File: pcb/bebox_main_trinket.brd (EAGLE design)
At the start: 92.8 x 35.2 mm, 25 parts, among them J1 SJ-435107RS, J2 SJ-435107RS, J4 SJ-435107RS, J6 PJ-102AH, P2 OSTTE020104, P3 OSTTE020104, P4 OSTTE020104, P5 OSTTE020104, T2 2SC2098V, T3 2SC2098V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

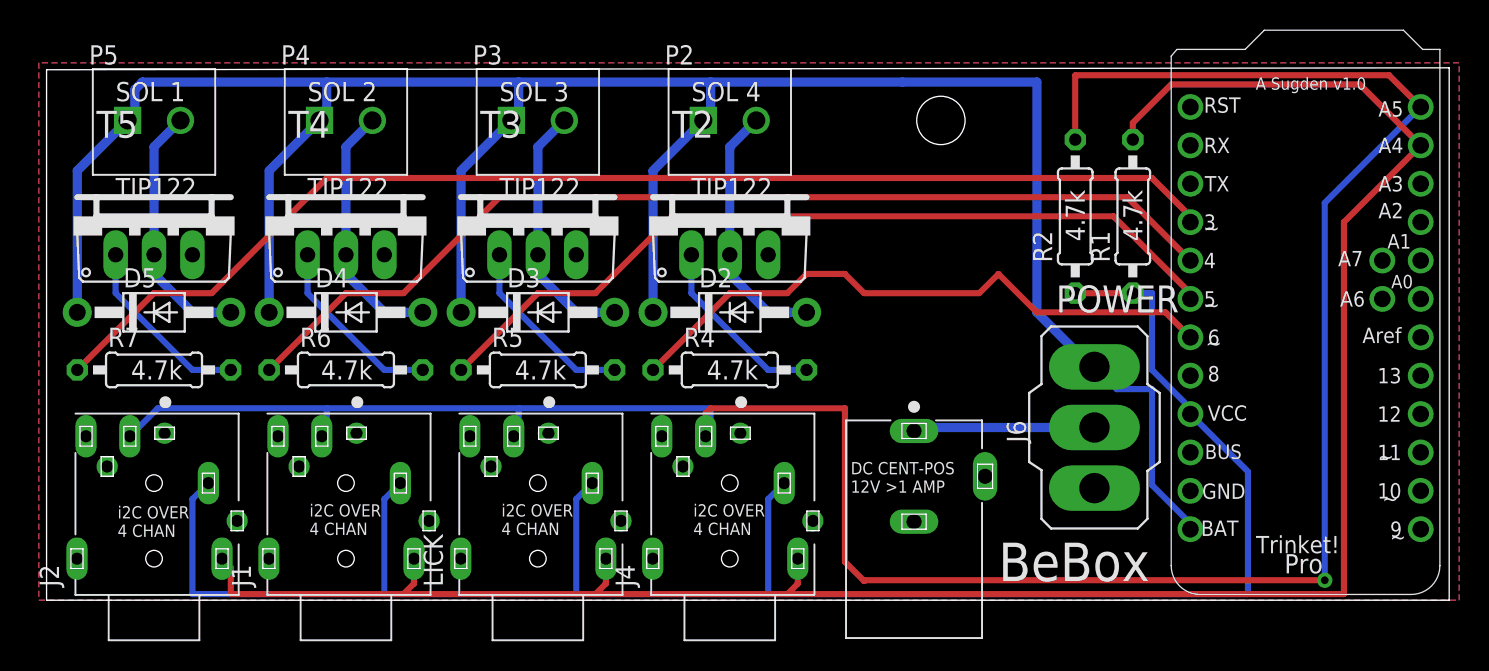
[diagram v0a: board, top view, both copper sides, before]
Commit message: Renamed original bebox main and udpated the  footprint of the switch.
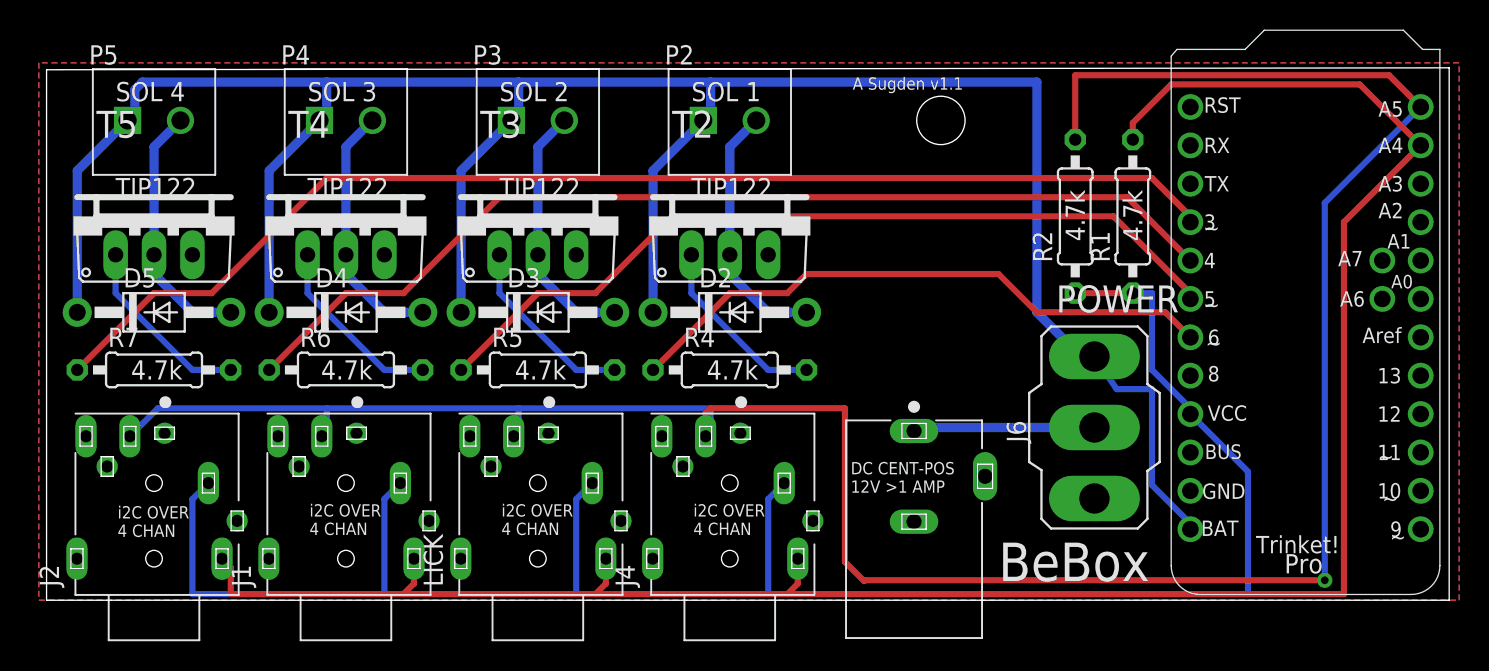
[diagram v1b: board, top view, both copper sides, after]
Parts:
- POWER: device switch:320-916 -> arthur:320-916
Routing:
- net N$15: track 41.0 -> 39.9 mm
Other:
- board text added: "A Sugden v1.1"
- board text removed: "A Sugden v1.0"
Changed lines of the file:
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@@
 <?xml version="1.0" encoding="utf-8"?>
 <!DOCTYPE eagle SYSTEM "eagle.dtd">
-<eagle version="9.3.0">
+<eagle version="9.3.2">
 <drawing>
 <settings>
@@
 <text x="13.97" y="36.83" size="1.27" layer="21">TIP122</text>
 <text x="72.39" y="11.43" size="2.54" layer="21">BeBox</text>
-<text x="89.408" y="43.942" size="0.8128" layer="21">A Sugden v1.0</text>
+<text x="62.738" y="43.942" size="0.8128" layer="21">A Sugden v1.1</text>
 <hole x="68.58" y="41.91" drill="3.199890625"/>
 <text x="14.097" y="14.351" size="0.8128" layer="21">i2C OVER
@@
 <text x="62.611" y="17.272" size="0.8128" layer="21">DC CENT-POS
 12V &gt;1 AMP</text>
-<text x="13.97" y="43.18" size="1.27" layer="21">SOL 1</text>
-<text x="26.67" y="43.18" size="1.27" layer="21">SOL 2</text>
-<text x="39.37" y="43.18" size="1.27" layer="21">SOL 3</text>
-<text x="52.07" y="43.18" size="1.27" layer="21">SOL 4</text>
+<text x="13.97" y="43.18" size="1.27" layer="21">SOL 4</text>
+<text x="26.67" y="43.18" size="1.27" layer="21">SOL 3</text>
+<text x="39.37" y="43.18" size="1.27" layer="21">SOL 2</text>
+<text x="52.07" y="43.18" size="1.27" layer="21">SOL 1</text>
 </plain>
 <attributes>
@@
 <attribute name="VALUE" x="12.20673125" y="36.706040625" size="1.27096875" layer="27"/>
 </element>
-<element name="POWER" library="switch" library_urn="urn:adsk.eagle:library:380" package="320-916" package3d_urn="urn:adsk.eagle:package:27678/1" value="" x="78.74" y="21.59" smashed="yes">
+<element name="POWER" library="arthur" package="320-916" package3d_urn="urn:adsk.eagle:package:27678/1" value="" x="78.74" y="21.59" smashed="yes">
 <attribute name="NAME" x="76.2" y="29.21" size="1.778" layer="25" ratio="10"/>
 <attribute name="VALUE" x="76.2" y="12.065" size="1.778" layer="27" ratio="10"/>
@@
 <wire x1="14.76" y1="41.91" x2="15.24" y2="42.39" width="0.6096" layer="16"/>
 <wire x1="15.24" y1="42.39" x2="15.24" y2="43.949509375" width="0.6096" layer="16"/>
-<wire x1="74.93" y1="29.21" x2="74.93" y2="44.45" width="0.6096" layer="16"/>
-<wire x1="74.93" y1="29.21" x2="78.5368" y2="25.6032" width="0.6096" layer="16"/>
-<wire x1="78.5368" y1="25.6032" x2="78.74" y2="25.6032" width="0.6096" layer="16"/>
+<wire x1="74.93" y1="44.45" x2="74.93" y2="29.21" width="0.6096" layer="16"/>
 <wire x1="15.740490625" y1="44.45" x2="15.24" y2="43.949509375" width="0.6096" layer="16"/>
-<wire x1="78.74" y1="25.6032" x2="80.2132" y2="24.13" width="0.4064" layer="16"/>
+<wire x1="78.74" y1="26.289" x2="80.2132" y2="24.13" width="0.4064" layer="16"/>
 <wire x1="80.2132" y1="24.13" x2="82.55" y2="24.13" width="0.4064" layer="16"/>
 <wire x1="82.55" y1="24.13" x2="82.55" y2="17.78" width="0.4064" layer="16"/>
@@
 <wire x1="49.53" y1="29.21" x2="49.53" y2="38.58" width="0.6096" layer="16"/>
 <wire x1="49.53" y1="38.58" x2="52.86" y2="41.91" width="0.6096" layer="16"/>
-<wire x1="74.93" y1="44.45" x2="66.04" y2="44.45" width="0.6096" layer="16"/>
-<wire x1="66.04" y1="44.45" x2="53.34" y2="44.45" width="0.6096" layer="16"/>
+<wire x1="74.93" y1="44.45" x2="53.34" y2="44.45" width="0.6096" layer="16"/>
 <wire x1="53.34" y1="44.45" x2="40.64" y2="44.45" width="0.6096" layer="16"/>
 <wire x1="40.64" y1="44.45" x2="27.94" y2="44.45" width="0.6096" layer="16"/>
@@
 <wire x1="40.16" y1="41.91" x2="40.64" y2="42.39" width="0.6096" layer="16"/>
 <wire x1="40.64" y1="42.39" x2="40.64" y2="44.45" width="0.6096" layer="16"/>
+<wire x1="74.93" y1="29.21" x2="77.851" y2="26.289" width="0.6096" layer="16"/>
+<wire x1="77.851" y1="26.289" x2="78.74" y2="26.289" width="0.6096" layer="16"/>
 </signal>
 <signal name="SDA">
@@
 <contactref element="U$1" pad="6"/>
 <wire x1="74.93" y1="29.21" x2="83.439" y2="29.21" width="0.4064" layer="1"/>
-<wire x1="74.93" y1="29.21" x2="72.39" y2="31.75" width="0.4064" layer="1"/>
-<wire x1="72.39" y1="31.75" x2="71.12" y2="30.48" width="0.4064" layer="1"/>
-<wire x1="71.12" y1="30.48" x2="63.5" y2="30.48" width="0.4064" layer="1"/>
-<wire x1="63.5" y1="30.48" x2="62.23" y2="31.75" width="0.4064" layer="1"/>
-<wire x1="62.23" y1="31.75" x2="59.69" y2="31.75" width="0.4064" layer="1"/>
-<wire x1="59.69" y1="31.75" x2="58.42" y2="30.48" width="0.4064" layer="1"/>
-<wire x1="58.42" y1="30.48" x2="54.61" y2="30.48" width="0.4064" layer="1"/>
+<wire x1="72.39" y1="31.75" x2="74.93" y2="29.21" width="0.4064" layer="1"/>
+<wire x1="54.61" y1="30.48" x2="58.42" y2="30.48" width="0.4064" layer="1"/>
 <wire x1="54.61" y1="30.48" x2="49.53" y2="25.4" width="0.4064" layer="1"/>
 <wire x1="83.439" y1="29.21" x2="85.09" y2="27.559" width="0.4064" layer="1"/>
+<wire x1="58.42" y1="30.48" x2="59.69" y2="31.75" width="0.4064" layer="1"/>
+<wire x1="59.69" y1="31.75" x2="72.39" y2="31.75" width="0.4064" layer="1"/>
 </signal>
 </signals>
